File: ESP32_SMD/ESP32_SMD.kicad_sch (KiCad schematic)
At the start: 95 parts, among them J1 POWER(5V), J10 INPUT_2, J11 Conn_01x02_Socket, J12 Conn_01x02_Socket, J13 Conn_01x02_Socket, J14 Conn_01x02_Socket, J15 Conn_01x03_Socket, J16 Conn_01x15_Socket, J17 I2C, J18 Conn_01x03_Socket, J19 Conn_01x03_Socket, J2 Conn_01x02_Socket, J20 Conn_01x15_Socket, J21 Conn_01x02_Socket, J22 Conn_01x03_Socket, J23 Conn_01x03_Socket, J24 Conn_01x03_Socket, J25 POWER(3.3V), J3 FT234X, J4 I2C, J5 Conn_01x02_Socket, J6 Conn_01x02_Socket, J7 Conn_01x02_Socket, J8 Conn_01x02_Socket, J9 INPUT_1, SW1 SW_Nidec_CAS-120A1, SW2 BOOT, SW3 EN, U1 ESP32-WROOM-32E, U2 NJM2845DL1-33

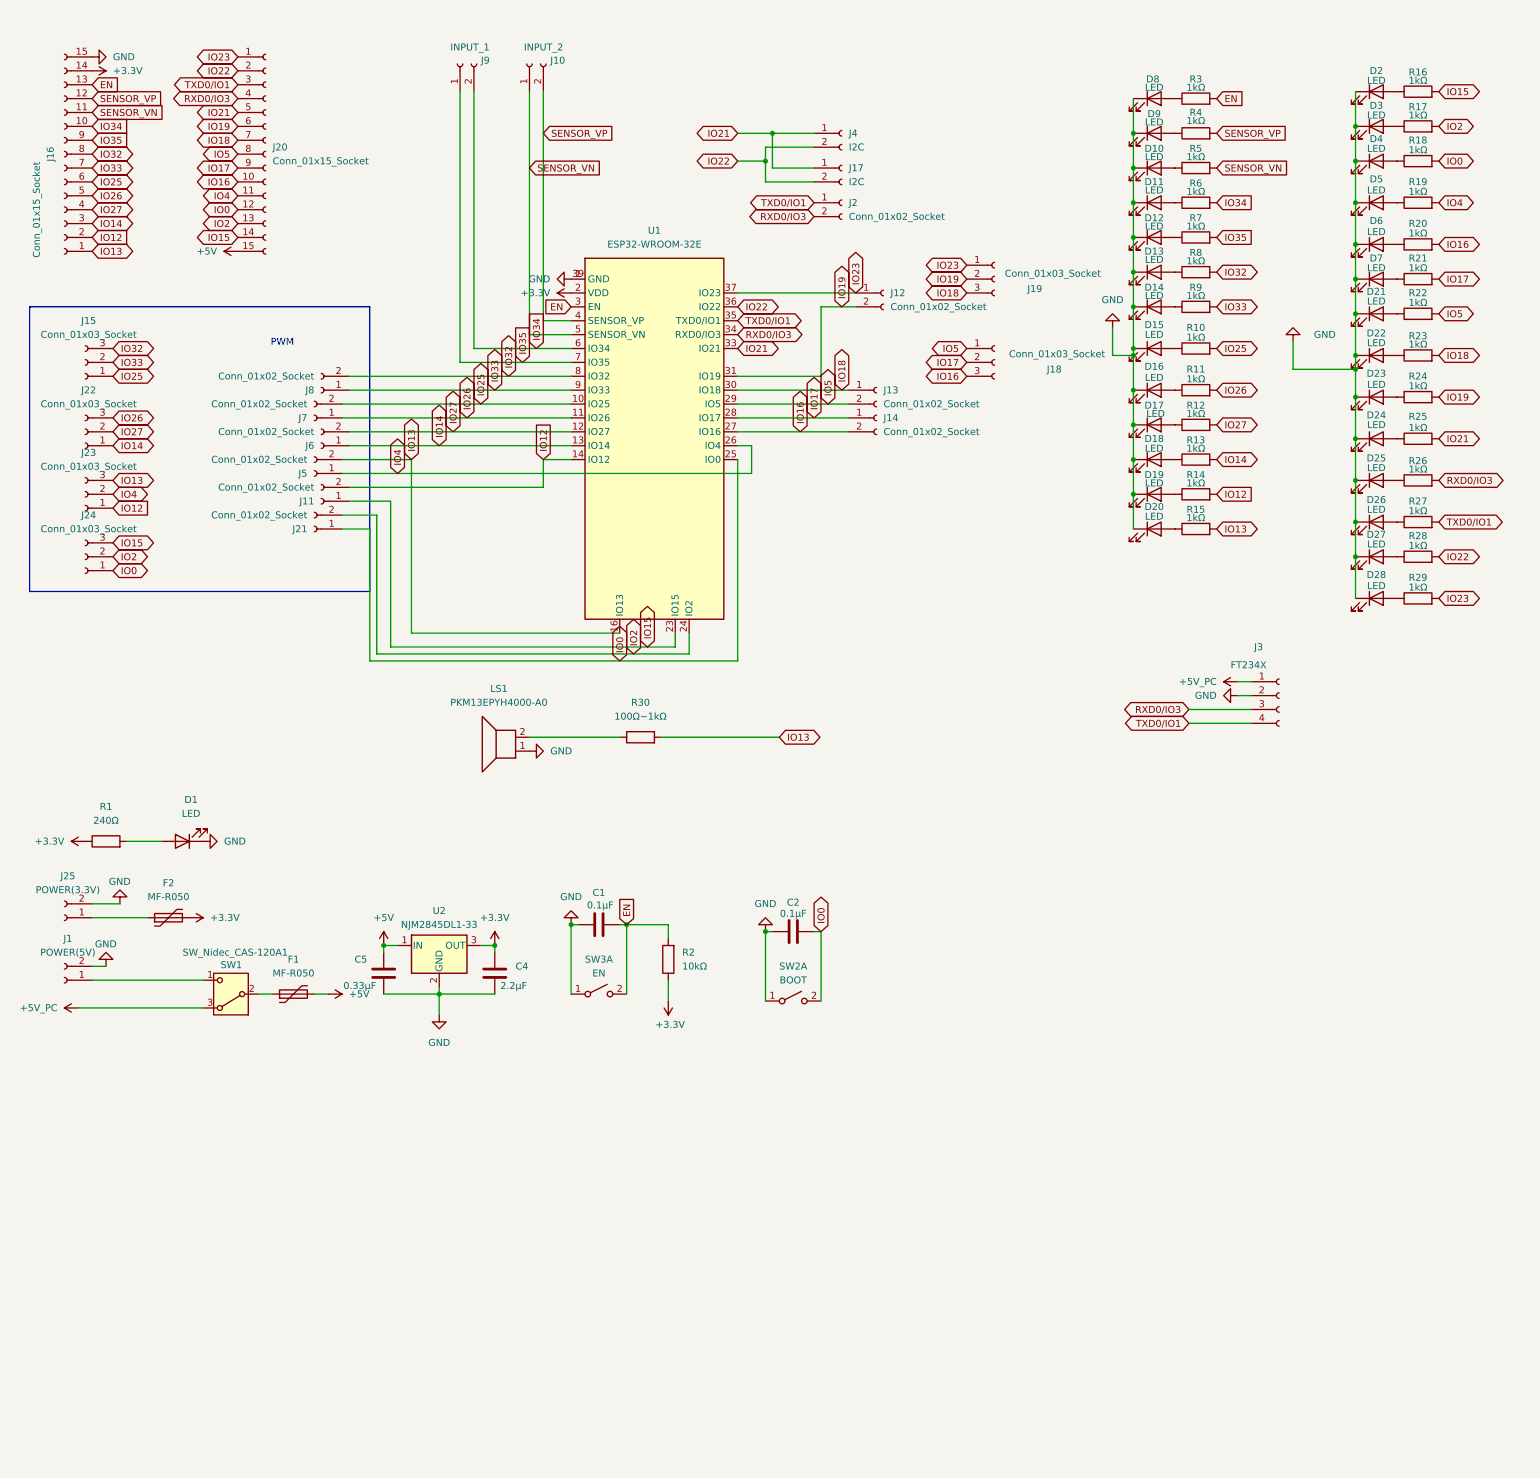
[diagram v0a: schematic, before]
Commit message: USB-cポートとシリアル変換を乗せた
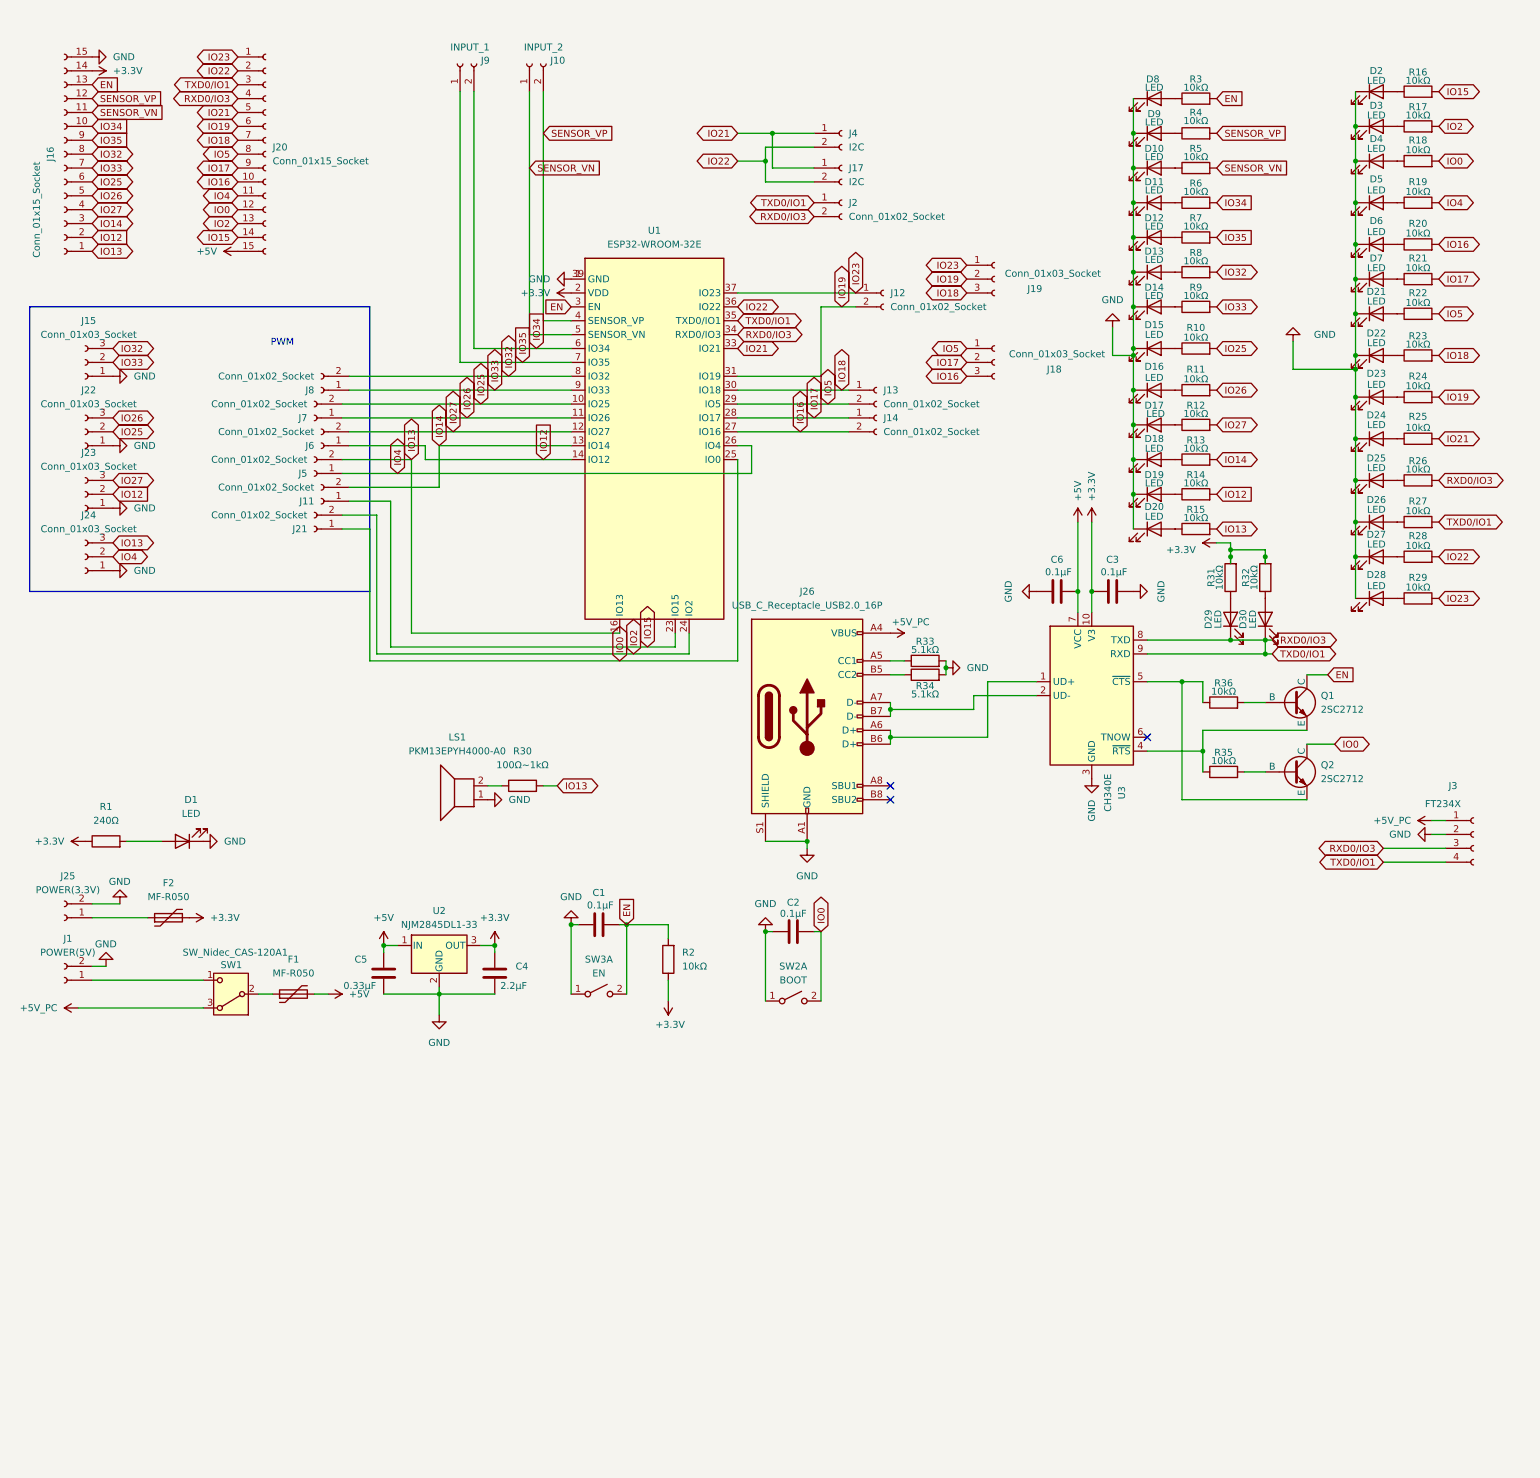
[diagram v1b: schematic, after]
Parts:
- added C3, C6: 0.1μF, Capacitor_SMD:C_0603_1608Metric_Pad1.08x0.95mm_HandSolder, symbol Device:C
- added D29, D30: LED, LED_SMD:LED_0603_1608Metric_Pad1.05x0.95mm_HandSolder, symbol Device:LED
- added J26: USB_C_Receptacle_USB2.0_16P, Connector_USB:USB_C_Receptacle_GCT_USB4105-xx-A_16P_TopMnt_Horizontal, symbol Connector:USB_C_Receptacle_USB2.0_16P
- added Q1, Q2: 2SC2712, Package_TO_SOT_SMD:SOT-23, symbol Simulation_SPICE:NPN
- added R31, R32, R35, R36: 10kΩ, Resistor_SMD:R_0603_1608Metric_Pad0.98x0.95mm_HandSolder, symbol Device:R
- added R33, R34: 5.1kΩ, Resistor_SMD:R_0603_1608Metric_Pad0.98x0.95mm_HandSolder, symbol Device:R
- added U3: CH340E, Package_SO:MSOP-10_3x3mm_P0.5mm, symbol Interface_USB:CH340E
- R10, R11, R12, R13, R14, R15, R16, R17, R18, R19, R20, R21, R22, R23, R24, R25, R26, R27, R28, R29, R3, R4, R5, R6, R7, R8, R9: value 1kΩ -> 10kΩ
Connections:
- net TXD0/IO1 is gone; now on net RXD0/IO3: J2.1 (Pin_1), J20.3 (Pin_3), J3.4 (RxD), R27.2, U1.35 (TXD0/IO1)
- net +3.3V: now also C3.2, R31.2, R32.2, U3.10 (V3)
- net +5V: now also C6.1, U3.7 (VCC)
- net +5V_PC: now also J26.A4 (VBUS), J26.A9 (VBUS), J26.B4 (VBUS), J26.B9 (VBUS)
- net EN: now also Q1.1 (C)
- net GND: now also J15.1 (Pin_1), J22.1 (Pin_1), J23.1 (Pin_1), J24.1 (Pin_1), C3.1, C6.2, J26.A1 (GND), J26.A12 (GND), J26.B1 (GND), J26.B12 (GND), J26.S1 (SHIELD), R33.2, R34.2, U3.3 (GND)
- net IO0: now also Q2.1 (C); no longer J24.1 (Pin_1)
- net IO12: now also J23.2 (Pin_2), J6.1 (Pin_1); no longer J11.2 (Pin_2), J23.1 (Pin_1)
- net IO13: now also J24.3 (Pin_3); no longer J23.3 (Pin_3)
- net IO14: now also J11.2 (Pin_2); no longer J22.1 (Pin_1), J6.1 (Pin_1)
- net IO15: no longer J24.3 (Pin_3)
- net IO2: no longer J24.2 (Pin_2)
- net IO25: now also J22.2 (Pin_2); no longer J15.1 (Pin_1)
- net IO27: now also J23.3 (Pin_3); no longer J22.2 (Pin_2)
- net IO4: now also J24.2 (Pin_2); no longer J23.2 (Pin_2)
- net RXD0/IO3: now also D29.1 (K), D30.1 (K), U3.8 (TXD), U3.9 (RXD)
- new net: D30.2 (A), R32.1
- new net: J26.A5 (CC1), R33.1
- new net: Q2.2 (B), R35.2
- new net: Q2.3 (E), R36.1, U3.5 (~{CTS})
- new net: J26.A6 (D+), J26.B6 (D+), U3.1 (UD+)
- new net: J26.A7 (D-), J26.B7 (D-), U3.2 (UD-)
- new net: J26.B5 (CC2), R34.1
- new net: D29.2 (A), R31.1
- new net: Q1.2 (B), R36.2
- new net: Q1.3 (E), R35.1, U3.4 (~{RTS})
- no-connect marks 0 -> 3
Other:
- moved on the sheet: J3, LS1, R30

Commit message: 2.1.0
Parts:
- removed D29, D30: LED, LED_SMD:LED_0603_1608Metric_Pad1.05x0.95mm_HandSolder, symbol Device:LED
- removed F2: MF-R050, 00a:MF-R050, symbol Device:Polyfuse
- removed J25: POWER(3.3V), Connector_JST:JST_XH_B2B-XH-A_1x02_P2.50mm_Vertical, symbol Connector:Conn_01x02_Socket
- removed R31, R32: 10kΩ, Resistor_SMD:R_0603_1608Metric_Pad0.98x0.95mm_HandSolder, symbol Device:R
- added C7: 22μF, Capacitor_SMD:C_0603_1608Metric_Pad1.08x0.95mm_HandSolder, symbol Device:C
- added C8, C9: 100nF, Capacitor_SMD:C_0603_1608Metric_Pad1.08x0.95mm_HandSolder, symbol Device:C
- added J25, J27: RJ45_Shielded, Connector_RJ:RJ45_Amphenol_RJHSE5380, symbol Connector:RJ45_Shielded
- added JP3, JP4: Jumper_2_Open, Connector_PinHeader_2.54mm:PinHeader_1x02_P2.54mm_Vertical, symbol Jumper:Jumper_2_Open
- added R37: 120Ω, Resistor_SMD:R_0603_1608Metric_Pad0.98x0.95mm_HandSolder, symbol Device:R
- added U4: ATA6561, Package_SO:SOP-8_3.9x4.9mm_P1.27mm, symbol 00a:ATA6561
- J16, J20: footprint Connector_PinHeader_2.54mm:PinHeader_1x15_P2.54mm_Vertical -> Connector_PinSocket_2.54mm:PinSocket_1x15_P2.54mm_Vertical
- R30: value 100Ω~1kΩ -> 240Ω
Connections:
- net +3.3V: now also C9.2, U4.8 (VIO)
- net +5V: now also C7.2, C8.2, U4.3 (VCC)
- net GND: now also C7.1, C8.1, C9.1, J25.SH, J27.SH, U4.2 (GND), U4.5 (STBY)
- net IO0: now also J21.2 (Pin_2), R30.2; no longer J21.1 (Pin_1)
- net IO13: no longer R30.2
- net IO18: now also J21.1 (Pin_1); no longer J13.1 (Pin_1)
- net IO2: now also J24.2 (Pin_2), J5.1 (Pin_1); no longer J21.2 (Pin_2)
- net IO4: now also J13.1 (Pin_1), U4.4 (RXD); no longer J24.2 (Pin_2), J5.1 (Pin_1)
- net IO5: now also U4.1 (TXD)
- net RXD0/IO3: no longer J2.1 (Pin_1), J20.3 (Pin_3), J3.4 (RxD), R27.2, U1.35 (TXD0/IO1), U3.9 (RXD)
- new net: J25.1, J27.1, JP3.2 (B), U4.6 (CANH)
- new net: J25.2, J27.2, JP4.1 (A), U4.7 (CANL)
- new net: JP3.1 (A), R37.2
- new net: JP4.2 (B), R37.1
- new net TXD0/IO1: J2.1 (Pin_1), J20.3 (Pin_3), J3.4 (RxD), R27.2, U1.35 (TXD0/IO1), U3.9 (RXD)
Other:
- note added: "確認用LED"
- moved on the sheet: D10, D11, D12, D13, D14, D15, D16, D17, D18, D19, D2, D20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

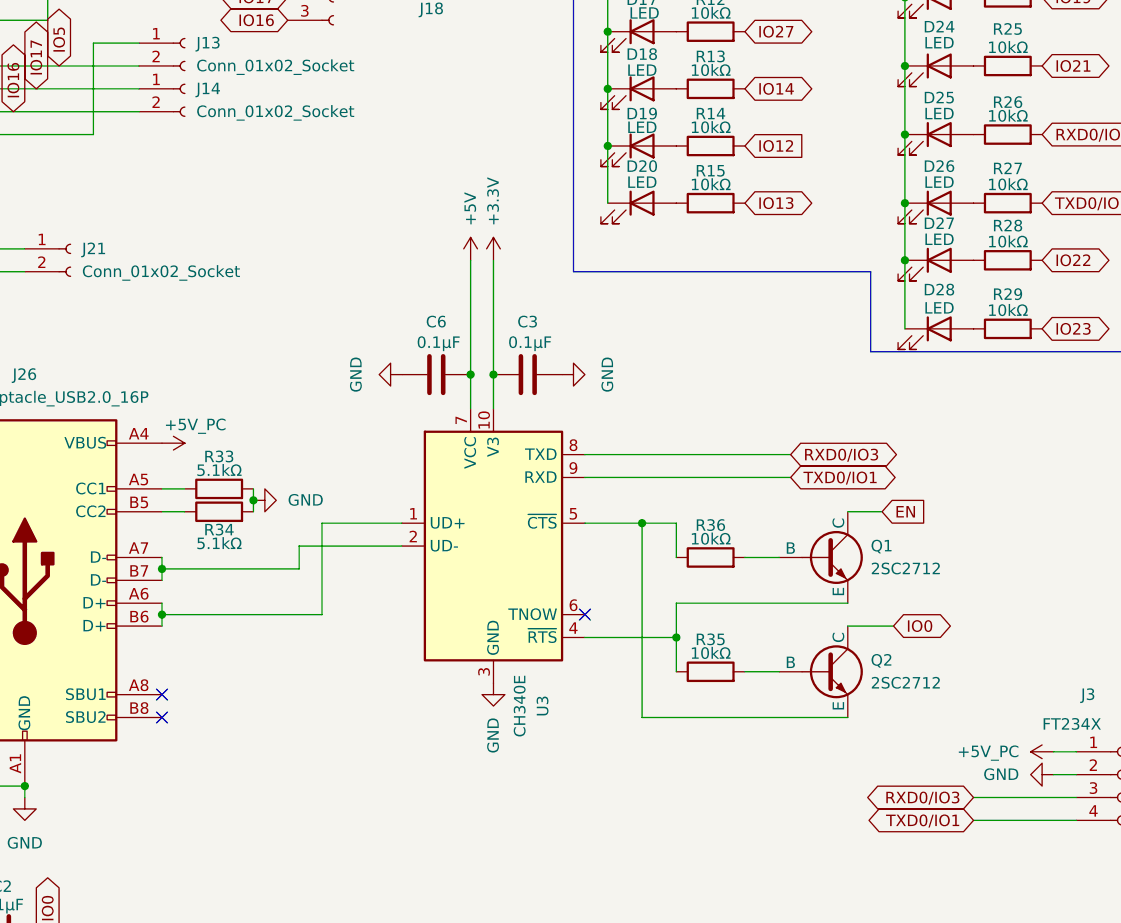
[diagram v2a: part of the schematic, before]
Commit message: RJ45フットプリント修正,CH340E→CH340K
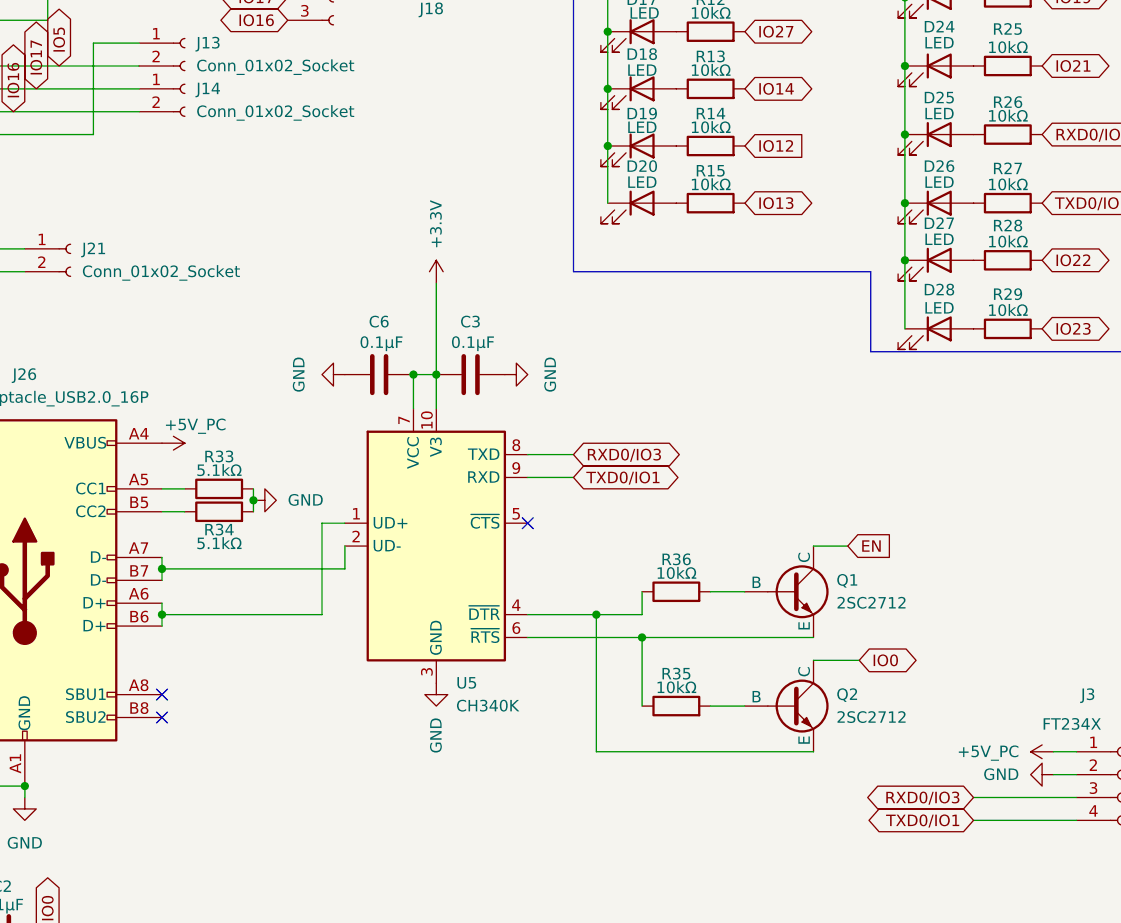
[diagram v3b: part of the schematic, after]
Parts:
- removed U3: CH340E, Package_SO:MSOP-10_3x3mm_P0.5mm, symbol Interface_USB:CH340E
- added U5: CH340K, Package_SO:SSOP-10-1EP_3.9x4.9mm_P1mm_EP2.1x3.3mm, symbol Interface_USB:CH340K
- J25, J27: footprint Connector_RJ:RJ45_Amphenol_RJHSE5380 -> 00a:RJ45
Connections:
- net +3.3V: now also C6.1, U5.10 (V3), U5.7 (VCC)
- net +5V: no longer C6.1
- net GND: now also U5.11 (GND), U5.3 (GND)
- net RXD0/IO3: now also U5.8 (TXD)
- net TXD0/IO1: now also U5.9 (RXD)
- net at Q2.3 (E), R36.1: now also U5.4 (~{DTR})
- net at J26.A6 (D+), J26.B6 (D+): now also U5.1 (UD+)
- net at J26.A7 (D-), J26.B7 (D-): now also U5.2 (UD-)
- net at Q1.3 (E), R35.1: now also U5.6 (~{RTS})
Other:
- moved on the sheet: C3, C6, Q1, Q2, R35, R36
